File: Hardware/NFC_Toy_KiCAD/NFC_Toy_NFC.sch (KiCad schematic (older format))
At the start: 29 parts

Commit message: Ready to start layout
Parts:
- added J18, J19: TP, symbol TEST_1P
- gave numbers to parts that had none: 29
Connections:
- no-connect marks 0 -> 16

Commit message: Layout started
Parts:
- removed J18, J19: TP, symbol TEST_1P
- added TP12, TP13: TEST, NFC_Toy_Lib:Test_Point, symbol TEST
- C17, C18, C21, C22, C23, C24, C25, C26, C28, C29, C30, C31, C32, C33, C34: footprint (none) -> Capacitors_SMD:C_0402
- C19, C20, C27: footprint (none) -> Capacitors_SMD:C_0603_HandSoldering
- L2, L3: footprint (none) -> Inductors_SMD:L_0603_HandSoldering
- R13, R14, R15, R16, R17, R18, R19: footprint (none) -> Resistors_SMD:R_0603_HandSoldering
- U5: footprint MODULE -> NFC_Toy_Lib:HVQFN40-6X6
- Y1: footprint ECS_ECS-100-18-20BQ-DS -> NFC_Toy_Lib:OSCCC500X320X105N
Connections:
- wire segments 100 -> 101

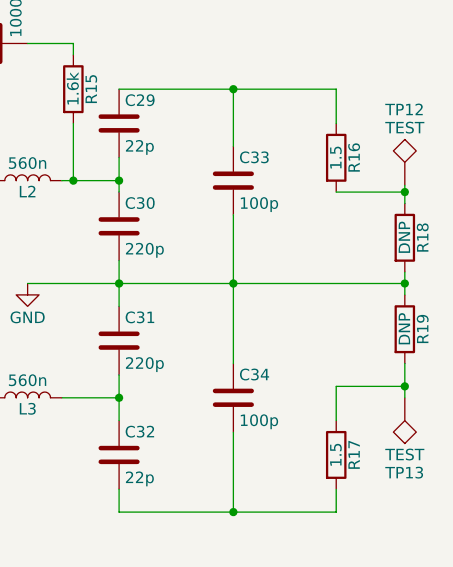
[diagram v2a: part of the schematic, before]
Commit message: Component placement complete.
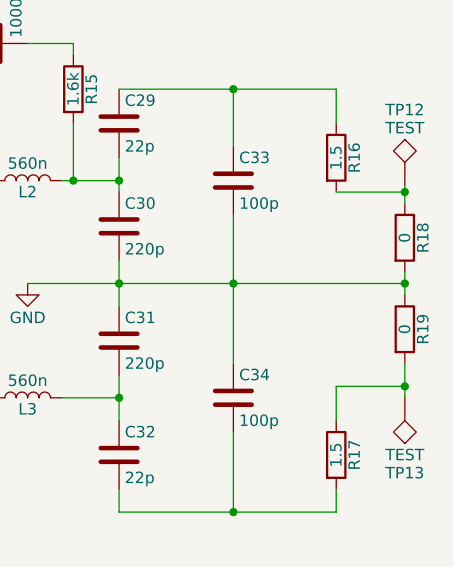
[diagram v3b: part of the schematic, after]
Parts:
- R18, R19: value DNP -> 0; footprint Resistors_SMD:R_0603_HandSoldering -> Resistors_SMD:R_0402
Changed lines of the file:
@@
 LIBS:APA102
 LIBS:SN74LVC2T45
+LIBS:mechanical
 LIBS:NFC_Toy-cache
 EELAYER 25 0
@@
 $EndComp
 $Comp
-L +3.3V #PWR047
+L +3.3V #PWR043
 U 1 1 5ACE3D82
 P 4900 1600
-F 0 "#PWR047" H 4900 1450 50  0001 C CNN
+F 0 "#PWR043" H 4900 1450 50  0001 C CNN
 F 1 "+3.3V" H 4900 1740 50  0000 C CNN
 F 2 "" H 4900 1600 50  0001 C CNN
@@
 $EndComp
 $Comp
-L GND #PWR048
+L GND #PWR044
 U 1 1 5ACE3D89
 P 4950 5750
-F 0 "#PWR048" H 4950 5500 50  0001 C CNN
+F 0 "#PWR044" H 4950 5500 50  0001 C CNN
 F 1 "GND" H 4950 5600 50  0000 C CNN
 F 2 "" H 4950 5750 50  0001 C CNN
@@
 Connection ~ 4900 1600
 $Comp
-L VCC #PWR049
+L VCC #PWR045
 U 1 1 5ACE4998
 P 7550 1650
-F 0 "#PWR049" H 7550 1500 50  0001 C CNN
+F 0 "#PWR045" H 7550 1500 50  0001 C CNN
 F 1 "VCC" H 7550 1800 50  0000 C CNN
 F 2 "" H 7550 1650 50  0001 C CNN
@@
 $EndComp
 $Comp
-L PWR_FLAG #FLG050
+L PWR_FLAG #FLG046
 U 1 1 5ACE49B0
 P 7550 1750
-F 0 "#FLG050" H 7550 1825 50  0001 C CNN
+F 0 "#FLG046" H 7550 1825 50  0001 C CNN
 F 1 "PWR_FLAG" H 7550 1900 50  0000 C CNN
 F 2 "" H 7550 1750 50  0001 C CNN
@@
 	7550 1650 7550 1750
 $Comp
-L VCC #PWR051
+L VCC #PWR047
 U 1 1 5ACE49E2
 P 5250 1800
-F 0 "#PWR051" H 5250 1650 50  0001 C CNN
+F 0 "#PWR047" H 5250 1650 50  0001 C CNN
 F 1 "VCC" H 5250 1950 50  0000 C CNN
 F 2 "" H 5250 1800 50  0001 C CNN
@@
 $EndComp
 $Comp
-L GND #PWR052
+L GND #PWR048
 U 1 1 5ACEB7BE
 P 6950 4000
-F 0 "#PWR052" H 6950 3750 50  0001 C CNN
+F 0 "#PWR048" H 6950 3750 50  0001 C CNN
 F 1 "GND" H 6950 3850 50  0000 C CNN
 F 2 "" H 6950 4000 50  0001 C CNN
@@
 P 8600 3800
 F 0 "R18" V 8680 3800 50  0000 C CNN
-F 1 "DNP" V 8600 3800 50  0000 C CNN
-F 2 "Resistors_SMD:R_0603_HandSoldering" V 8530 3800 50  0001 C CNN
+F 1 "0" V 8600 3800 50  0000 C CNN
+F 2 "Resistors_SMD:R_0402" V 8530 3800 50  0001 C CNN
 F 3 "" H 8600 3800 50  0001 C CNN
 	1    8600 3800
@@
 P 8600 4200
 F 0 "R19" V 8680 4200 50  0000 C CNN
-F 1 "DNP" V 8600 4200 50  0000 C CNN
-F 2 "Resistors_SMD:R_0603_HandSoldering" V 8530 4200 50  0001 C CNN
+F 1 "0" V 8600 4200 50  0000 C CNN
+F 2 "Resistors_SMD:R_0402" V 8530 4200 50  0001 C CNN
 F 3 "" H 8600 4200 50  0001 C CNN
 	1    8600 4200
@@
 	6250 3200 6100 3200
 $Comp
-L GND #PWR053
+L GND #PWR049
 U 1 1 5ACEC797
 P 6250 4650
-F 0 "#PWR053" H 6250 4400 50  0001 C CNN
+F 0 "#PWR049" H 6250 4400 50  0001 C CNN
 F 1 "GND" H 6250 4500 50  0000 C CNN
 F 2 "" H 6250 4650 50  0001 C CNN
@@
 	3200 2950 4000 2950
 $Comp
-L GND #PWR054
+L GND #PWR050
 U 1 1 5ACECF73
 P 3250 3450
-F 0 "#PWR054" H 3250 3200 50  0001 C CNN
+F 0 "#PWR050" H 3250 3200 50  0001 C CNN
 F 1 "GND" H 3250 3300 50  0000 C CNN
 F 2 "" H 3250 3450 50  0001 C CNN
@@
 	3250 3150 3250 3450
 $Comp
-L GND #PWR055
+L GND #PWR051
 U 1 1 5ACED04D
 P 1950 3200
-F 0 "#PWR055" H 1950 2950 50  0001 C CNN
+F 0 "#PWR051" H 1950 2950 50  0001 C CNN
 F 1 "GND" H 1950 3050 50  0000 C CNN
 F 2 "" H 1950 3200 50  0001 C CNN
@@
 Connection ~ 3450 2950
 $Comp
-L GND #PWR056
+L GND #PWR052
 U 1 1 5ACED8D4
 P 3900 3350
-F 0 "#PWR056" H 3900 3100 50  0001 C CNN
+F 0 "#PWR052" H 3900 3100 50  0001 C CNN
 F 1 "GND" H 3900 3200 50  0000 C CNN
 F 2 "" H 3900 3350 50  0001 C CNN
@@
 	3900 3250 4000 3250
 $Comp
-L +3.3V #PWR057
+L +3.3V #PWR053
 U 1 1 5ACEDB84
 P 3700 3150
-F 0 "#PWR057" H 3700 3000 50  0001 C CNN
+F 0 "#PWR053" H 3700 3000 50  0001 C CNN
 F 1 "+3.3V" H 3700 3290 50  0000 C CNN
 F 2 "" H 3700 3150 50  0001 C CNN
@@
 $EndComp
 $Comp
-L +3.3V #PWR058
+L +3.3V #PWR054
 U 1 1 5ACEF2AA
 P 3700 4750
-F 0 "#PWR058" H 3700 4600 50  0001 C CNN
+F 0 "#PWR054" H 3700 4600 50  0001 C CNN
 F 1 "+3.3V" H 3700 4890 50  0000 C CNN
 F 2 "" H 3700 4750 50  0001 C CNN
@@
 Connection ~ 4200 1650
 $Comp
-L GND #PWR059
+L GND #PWR055
 U 1 1 5ACF0B0F
 P 3900 2150
-F 0 "#PWR059" H 3900 1900 50  0001 C CNN
+F 0 "#PWR055" H 3900 1900 50  0001 C CNN
 F 1 "GND" H 3900 2000 50  0000 C CNN
 F 2 "" H 3900 2150 50  0001 C CNN
@@
 $EndComp
 $Comp
-L GND #PWR060
+L GND #PWR056
 U 1 1 5ACF0B6E
 P 6450 2300
-F 0 "#PWR060" H 6450 2050 50  0001 C CNN
+F 0 "#PWR056" H 6450 2050 50  0001 C CNN
 F 1 "GND" H 6450 2150 50  0000 C CNN
 F 2 "" H 6450 2300 50  0001 C CNN
@@
 $EndComp
 $Comp
-L GND #PWR061
+L GND #PWR057
 U 1 1 5ACF12FD
 P 3900 5700
-F 0 "#PWR061" H 3900 5450 50  0001 C CNN
+F 0 "#PWR057" H 3900 5450 50  0001 C CNN
 F 1 "GND" H 3900 5550 50  0000 C CNN
 F 2 "" H 3900 5700 50  0001 C CNN

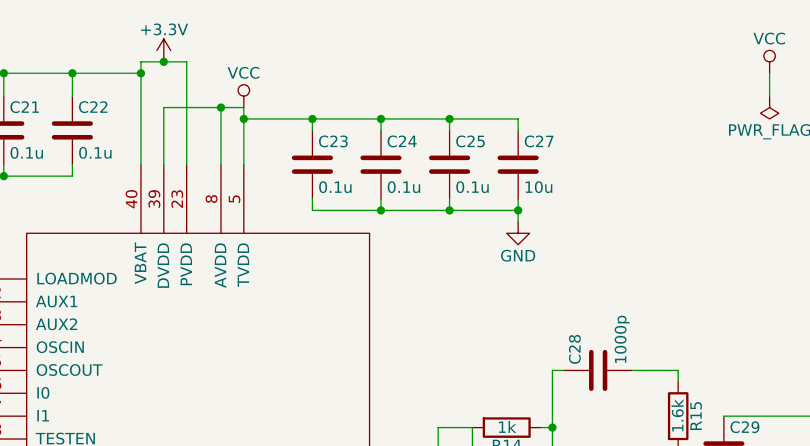
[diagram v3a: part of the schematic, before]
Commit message: Layout 75% complete
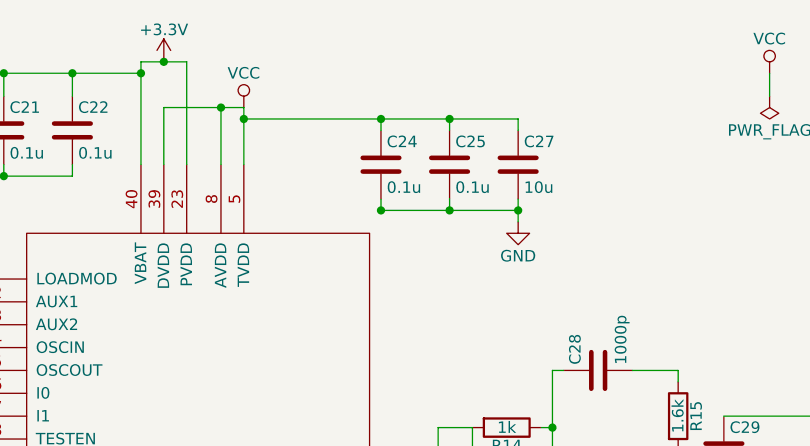
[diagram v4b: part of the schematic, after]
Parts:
- removed C23: 0.1u, Capacitors_SMD:C_0402, symbol C
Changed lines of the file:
@@
 Connection ~ 3700 5150
-$Comp
-L C C23
-U 1 1 5ACEFE58
-P 5550 2050
-F 0 "C23" H 5575 2150 50  0000 L CNN
-F 1 "0.1u" H 5575 1950 50  0000 L CNN
-F 2 "Capacitors_SMD:C_0402" H 5588 1900 50  0001 C CNN
-F 3 "" H 5550 2050 50  0001 C CNN
-	1    5550 2050
-	1    0    0    -1
-$EndComp
 $Comp
 L C C24
@@
 	1    0    0    -1
 $EndComp
-Wire Wire Line
-	5550 1850 5550 1900
 Connection ~ 5250 1850
 Wire Wire Line
 	5850 1850 5850 1900
-Connection ~ 5550 1850
 Wire Wire Line
 	6150 1850 6150 1900
@@
 Wire Wire Line
 	6450 2200 6450 2300
-Wire Wire Line
-	5550 2200 5550 2250
-Wire Wire Line
-	5550 2250 6450 2250
 Connection ~ 6450 2250
 Wire Wire Line
@@
 	-1   0    0    1
 $EndComp
+Wire Wire Line
+	5850 2250 6450 2250
 $EndSCHEMATC

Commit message: Added RNG and "Try Again"
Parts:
- C?: renamed from C30; symbol C -> Device:C
- C?: renamed from C31; symbol C -> Device:C
- C?: renamed from C29; symbol C -> Device:C
- C?: renamed from C32; symbol C -> Device:C
- C?: renamed from C34; symbol C -> Device:C
- C?: renamed from C33; symbol C -> Device:C
- C?: renamed from C28; symbol C -> Device:C
- C?: renamed from C26; symbol C -> Device:C
- C?: renamed from C17; symbol C -> Device:C
- C?: renamed from C18; symbol C -> Device:C
- C?: renamed from C24; symbol C -> Device:C
- C?: renamed from C25; symbol C -> Device:C
- C?: renamed from C21; symbol C -> Device:C
- C?: renamed from C22; symbol C -> Device:C
- C?: renamed from C27; symbol C -> Device:C
- C?: renamed from C19; symbol C -> Device:C
- C?: renamed from C20; symbol C -> Device:C
- L?: renamed from L2; symbol L -> Device:L
- L?: renamed from L3; symbol L -> Device:L
- R?: renamed from R17; symbol R -> Device:R
- R?: renamed from R16; symbol R -> Device:R
- R?: renamed from R18; symbol R -> Device:R
- R?: renamed from R19; symbol R -> Device:R
- R?: renamed from R15; symbol R -> Device:R
- R?: renamed from R14; symbol R -> Device:R
- R?: renamed from R13; symbol R -> Device:R
- TP?: renamed from TP12; symbol TEST -> NFC_Toy-rescue:TEST
- TP?: renamed from TP13; symbol TEST -> NFC_Toy-rescue:TEST
- U?: renamed from U5; symbol PN532 -> PN532:PN532
- Y?: renamed from Y1; symbol Oscillator -> Oscillator1:Oscillator
